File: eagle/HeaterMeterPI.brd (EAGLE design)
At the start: 94.6 x 45.7 mm, 63 parts, among them IC1 OKI-78SR-5, IC2 ATmega328P, IC4 MCP1700-33, IC5 AD849X, J1 RPi, J2 PROBE, J4 PCC-SMP, J9 POW, Q1 BS170, Q2 BS170, Q3 FQU11P06TU, Q5 BS170, Y1 16MHz

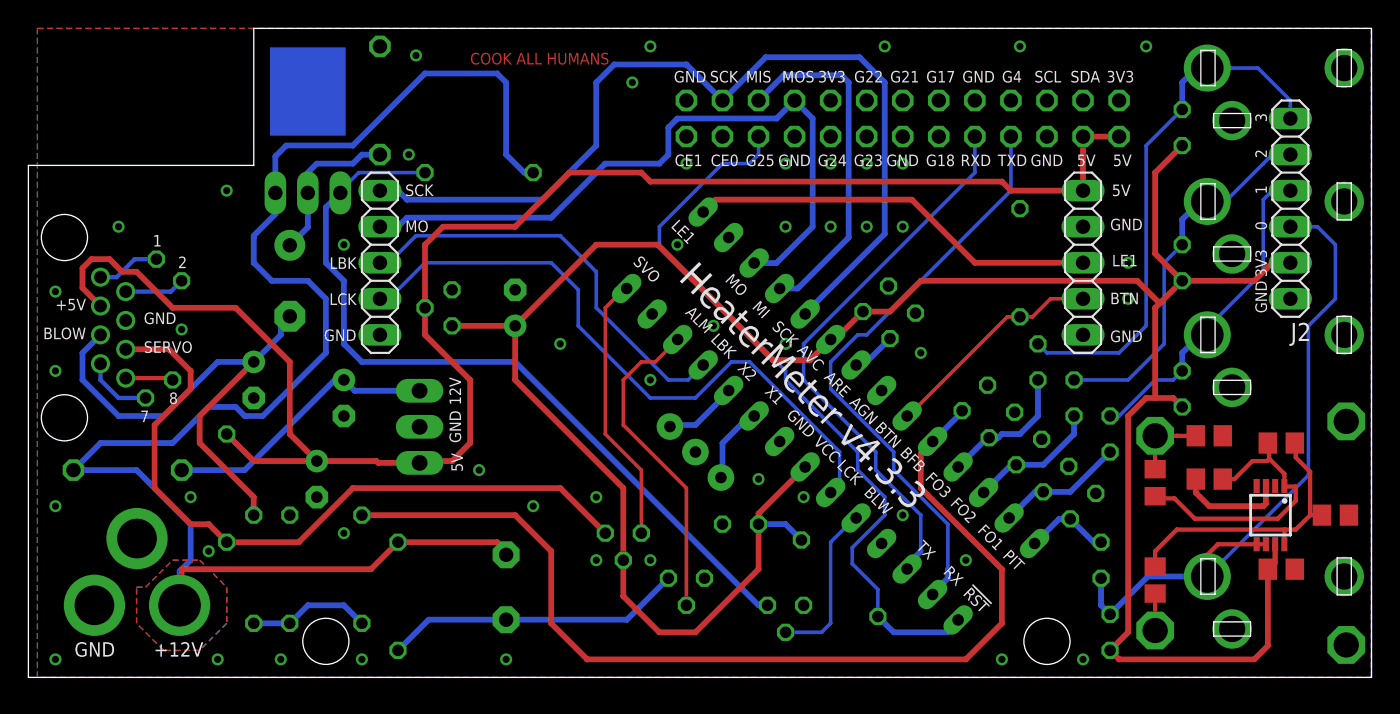
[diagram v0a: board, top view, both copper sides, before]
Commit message: [eagle] HeaterMeter 4.3.4
-- Base Board --
Increase annular ring to 14mil (from 7)
Increase thermal isolation to 15mil (from 10)
Chamfer corners on front edge
Rearrange power MOSFET footprint to sink more heat into board
Add TC+/- indicators to thermocouple pins
More direct path for 5V out and 12V in (swap D3 and R21)

-- LCD Board --
Add word "CONTRAST" by contrast pot
Increase annular ring to 14mil (from 12)
Increase thermals to 15mil (from 10)
Redo LCD1M labels to match labels of MOSI/SCK/etc on main
Add pin labels to shift register
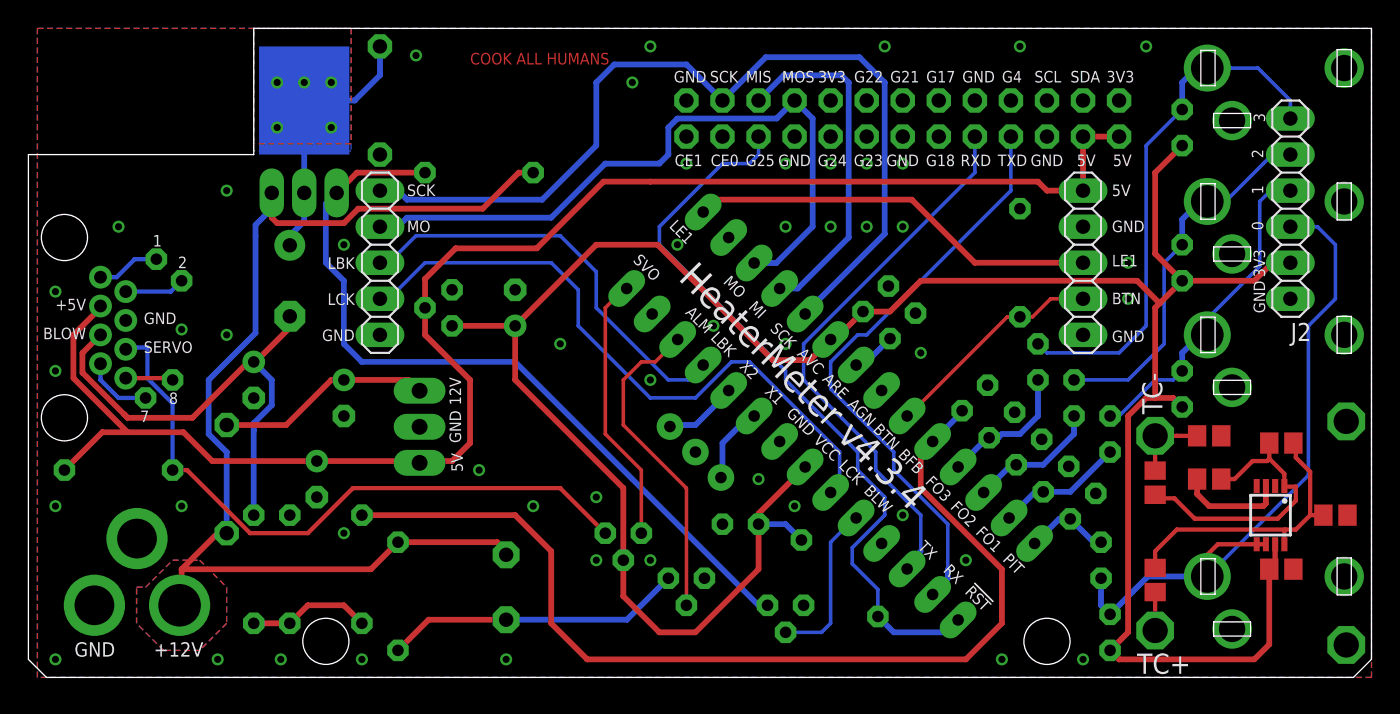
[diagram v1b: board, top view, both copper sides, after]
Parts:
- moved R21 7.73 mm to (5.71, 14.6), turned to 0 degrees
- moved D3 7.01 mm to (13.3, 14.0), turned to 270 degrees
- moved Q3 0.25 mm to (18.8, 36.8)
- turned D2 to 270 degrees
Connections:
- net N$4: now also Q3.2@1, Q3.2@2; no longer Q3.2
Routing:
- net +12V: track 108.9 -> 79.1 mm
- net +5V: track 119.0 -> 111.1 mm
- net N$4: track 11.3 -> 18.7 mm, vias 0 -> 5
- net SRVBST: track 50.7 -> 45.9 mm
- net VRM_IN: track 19.7 -> 15.2 mm
- net +12V_BLW: track 37.0 -> 34.8 mm
- net GND: track 7.60 -> 7.56 mm, vias 50 -> 49
- added copper zone on layer 1, net N$4
- added copper zone on layer 16, net N$4
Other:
- outline, holes or cut-outs redrawn
- board text added: "HeaterMeter v4.3.4"
- board text added: "TC+"
- board text added: "TC-"
- board text removed: "HeaterMeter v4.3.3"
